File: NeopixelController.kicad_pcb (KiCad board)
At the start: 2 copper layers, 63 x 30.5 mm, 22 parts, among them J1 Barrel_Jack_Switch, J2 Conn_01x16_Female, J3 Conn_01x12_Female, J4 Conn_01x03_Male, J5 Conn_01x03_Male, J6 Conn_01x04_Male, U1 74HCT125, U2 PLUG, U3 PLUG, U4 AP2112K-3.3

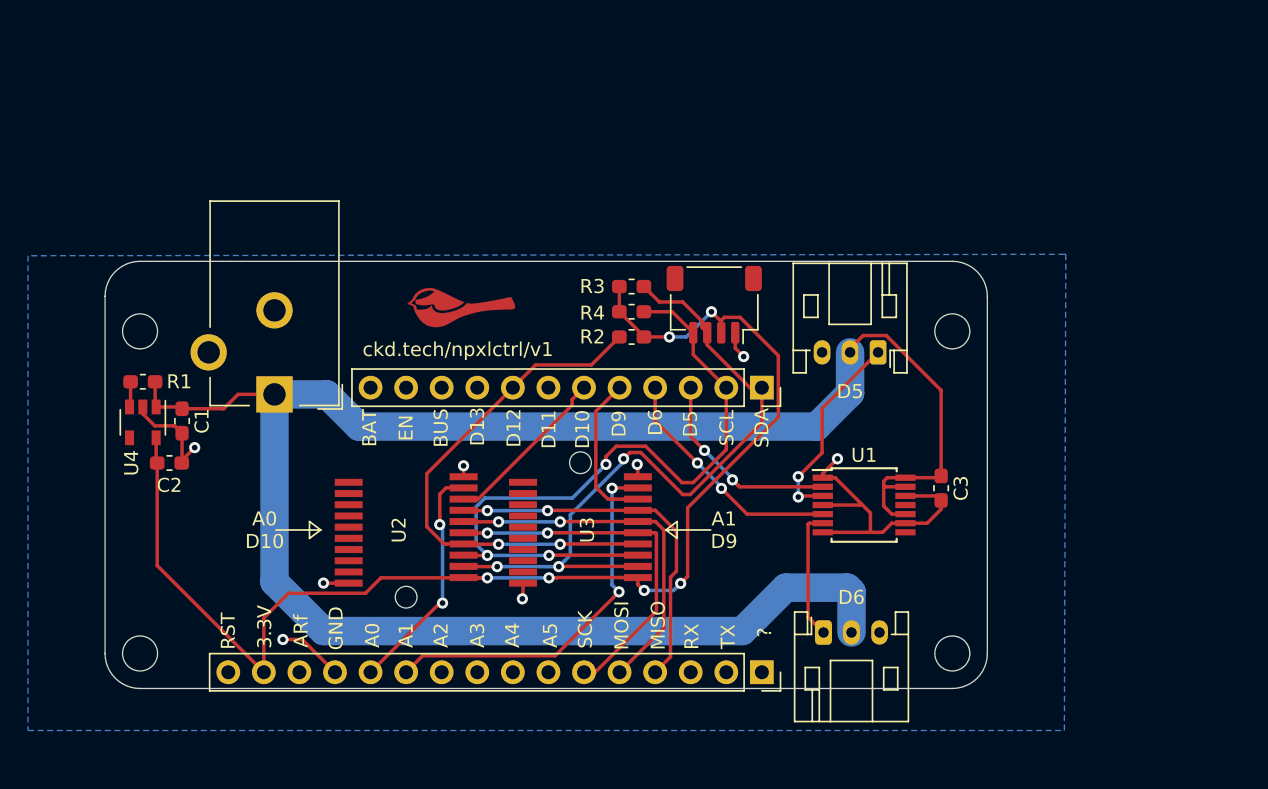
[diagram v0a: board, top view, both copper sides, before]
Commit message: V2 with four outputs
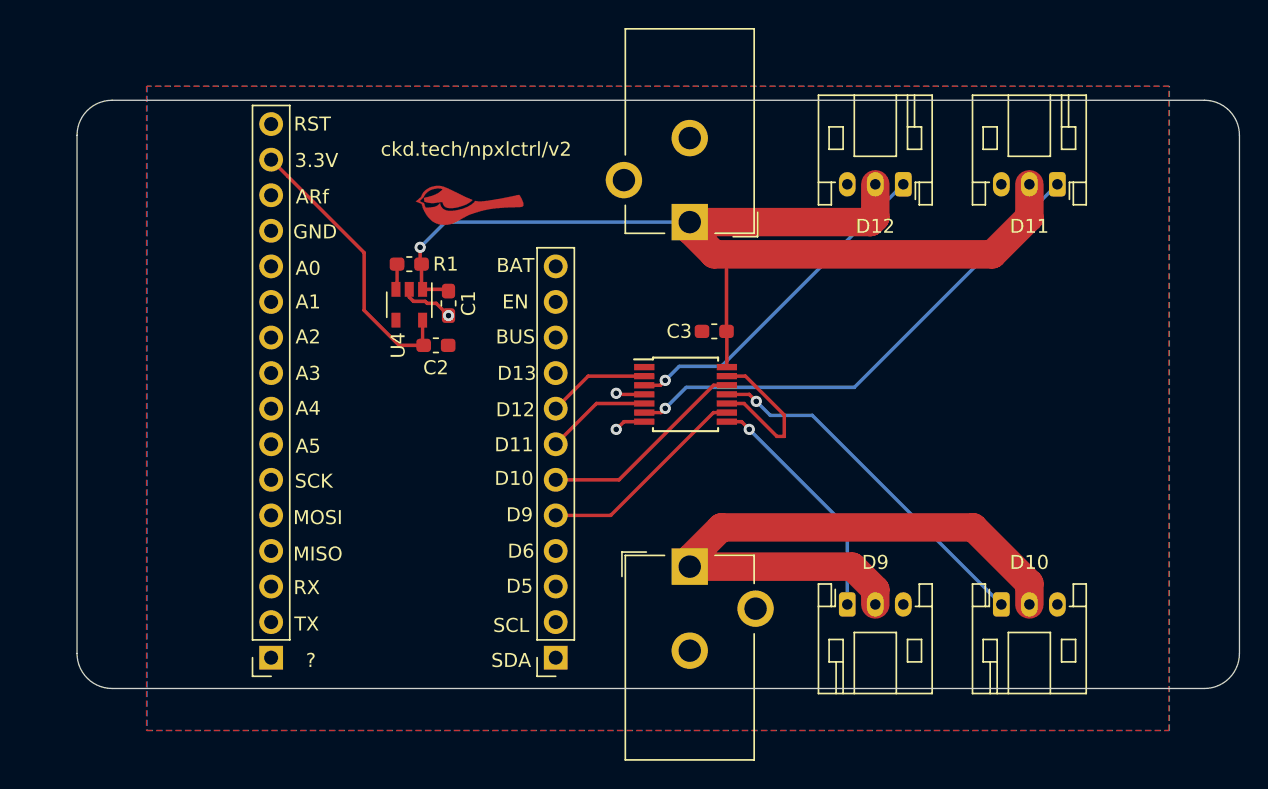
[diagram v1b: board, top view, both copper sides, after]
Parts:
- removed J6: Conn_01x04_Male, Connector_JST:JST_SH_SM04B-SRSS-TB_1x04-1MP_P1.00mm_Horizontal
- removed R2: 10k, Resistor_SMD:R_0603_1608Metric_Pad1.05x0.95mm_HandSolder
- removed R3, R4: 4.7k, Resistor_SMD:R_0603_1608Metric_Pad1.05x0.95mm_HandSolder
- removed REF** (x4): MountingHole_2.5mm, MountingHole:MountingHole_2.5mm
- removed U2, U3: PLUG, PLUG:PLUG
- added J7: Barrel_Jack_Switch, Connector_BarrelJack:BarrelJack_CUI_PJ-102AH_Horizontal, F.Cu at (147.2, 109.3)
- added J8: Conn_01x03_Male, Connector_JST:JST_PH_S3B-PH-K_1x03_P2.00mm_Horizontal, F.Cu at (158.5, 112.0)
- added J9: Conn_01x03_Male, Connector_JST:JST_PH_S3B-PH-K_1x03_P2.00mm_Horizontal, F.Cu at (169.5, 112.0)
- moved J4 36.1 mm to (173.5, 82.0), turned to 180 degrees
- moved J2 35.1 mm to (117.4, 115.8), turned to 180 degrees
- moved J1 32.1 mm to (147.2, 84.7)
- moved J3 24.3 mm to (137.7, 115.8), turned to 180 degrees
- moved C1 20.8 mm to (130.0, 90.5)
- moved C2 20.8 mm to (129.1, 93.5)
- moved U4 20.8 mm to (127.2, 90.6)
- moved R1 20.8 mm to (127.2, 87.7)
- moved C3 19.7 mm to (149.0, 92.5), turned to 180 degrees
- moved U1 15.0 mm to (146.9, 97.0)
- moved J5 12.1 mm to (162.5, 82.0)
- moved G*** 7.32 mm to (131.5, 83.5)
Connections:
- net +3V3 renamed +3.3V
- net /D5_5V renamed /D12_5V
- net /D6_5V renamed /D11_5V
- J1 pad 3: Net-(J1-Pad3) -> unconnected-(J1-Pad3)
- J2 pad 1: Net-(J2-Pad1) -> unconnected-(J2-Pin_1-Pad1)
- U1 pad 10: +5V -> GND
- U1 pad 11: Net-(U1-Pad11) -> /D10_5V
- U1 pad 12: GND -> /D10
- U1 pad 13: +5V -> GND
- U1 pad 2: /D5 -> /D12
- U1 pad 5: /D6 -> /D11
- U1 pad 8: Net-(U1-Pad8) -> /D9_5V
- U1 pad 9: GND -> /D9
- U4 pad 4: Net-(U4-Pad4) -> unconnected-(U4-NC-Pad4)
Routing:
- net +3.3V: track 94.4 -> 20.6 mm, vias 6 -> 0
- net +5V: track 141.4 -> 81.1 mm, vias 0 -> 1
- net /SCL: track 51.8 -> 0.00 mm, vias 3 -> 0
- net /SDA: track 50.2 -> 0.00 mm, vias 3 -> 0
- net +5VB: track 0.00 -> 43.9 mm
- net /D12: track 37.2 -> 7.28 mm, vias 2 -> 0
- net /A1: track 27.0 -> 0.00 mm, vias 2 -> 0
- net /D11_5V: track 9.26 -> 36.3 mm, vias 0 -> 1
- net /MISO: track 26.5 -> 0.00 mm, vias 2 -> 0
- net /SCK: track 26.3 -> 0.00 mm, vias 2 -> 0
- net /MOSI: track 26.0 -> 0.00 mm, vias 2 -> 0
- net /D10_5V: track 0.00 -> 25.8 mm, vias 0 -> 1
- net GND: track 41.9 -> 20.5 mm, vias 8 -> 3
- net /D9_5V: track 0.00 -> 17.2 mm, vias 0 -> 1
- net /D6: track 17.2 -> 0.00 mm, vias 2 -> 0
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- added copper zone on F.Cu, net GND
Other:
- board size 63 x 30.5 mm -> 83 x 42 mm
- net class Default removed
- rule pad_to_mask_clearance: 0.0508 -> 0.0762
- rule solder_mask_min_width: 0.25 -> 0.1016
- board text added: "ckd.tech/npxlctrl/v2"
- board text removed: "A0 D10"
- board text removed: "A1 D9"
- board text removed: "ckd.tech/npxlctrl/v1"
